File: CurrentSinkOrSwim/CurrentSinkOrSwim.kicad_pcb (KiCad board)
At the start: 2 copper layers, 41.7 x 47.8 mm, 23 parts, among them K101 CONN_3, P101 CONN_2, P102 CONN_2, P301 CONN_1, Q301 BUK7575, U201 LMV358, U401 LM2931ACDG

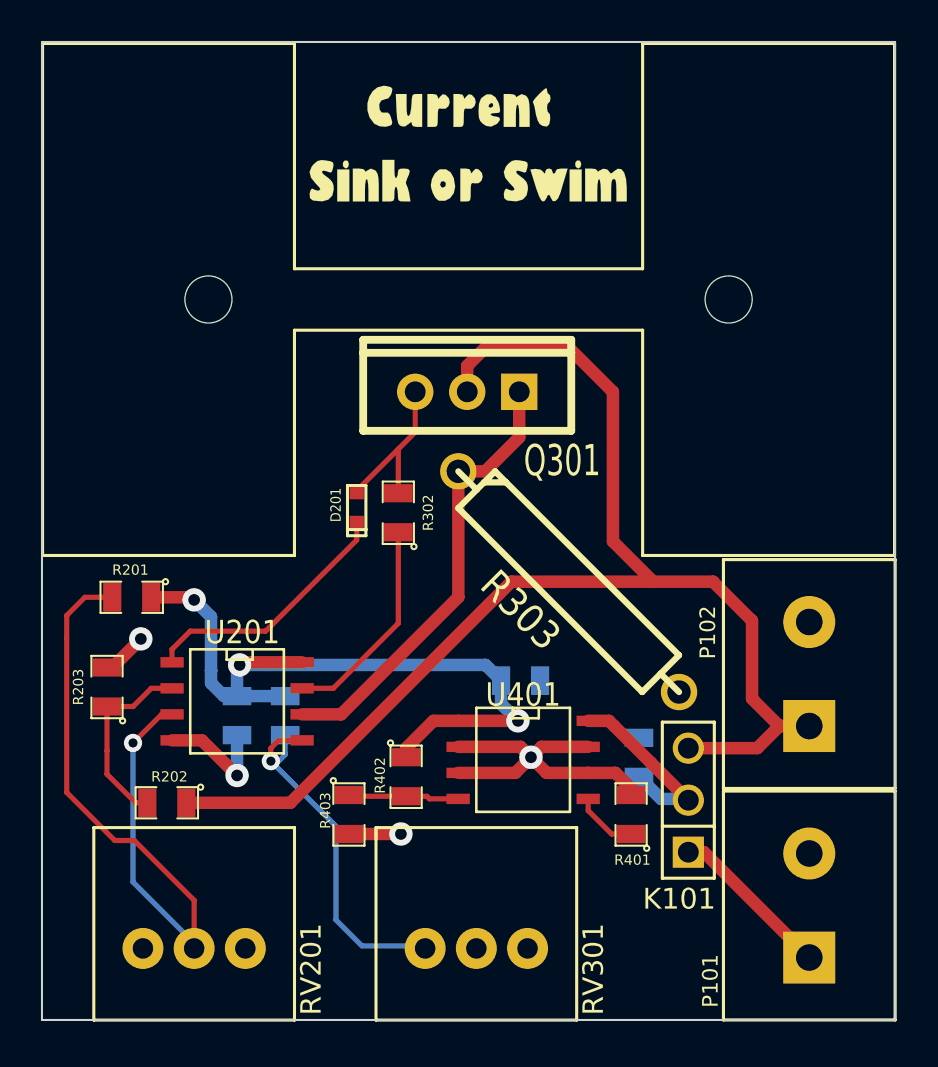
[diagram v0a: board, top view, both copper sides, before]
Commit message: Haciendo algunos cambios porque he tenido que cambiar de componentes y algún valor estaba mal
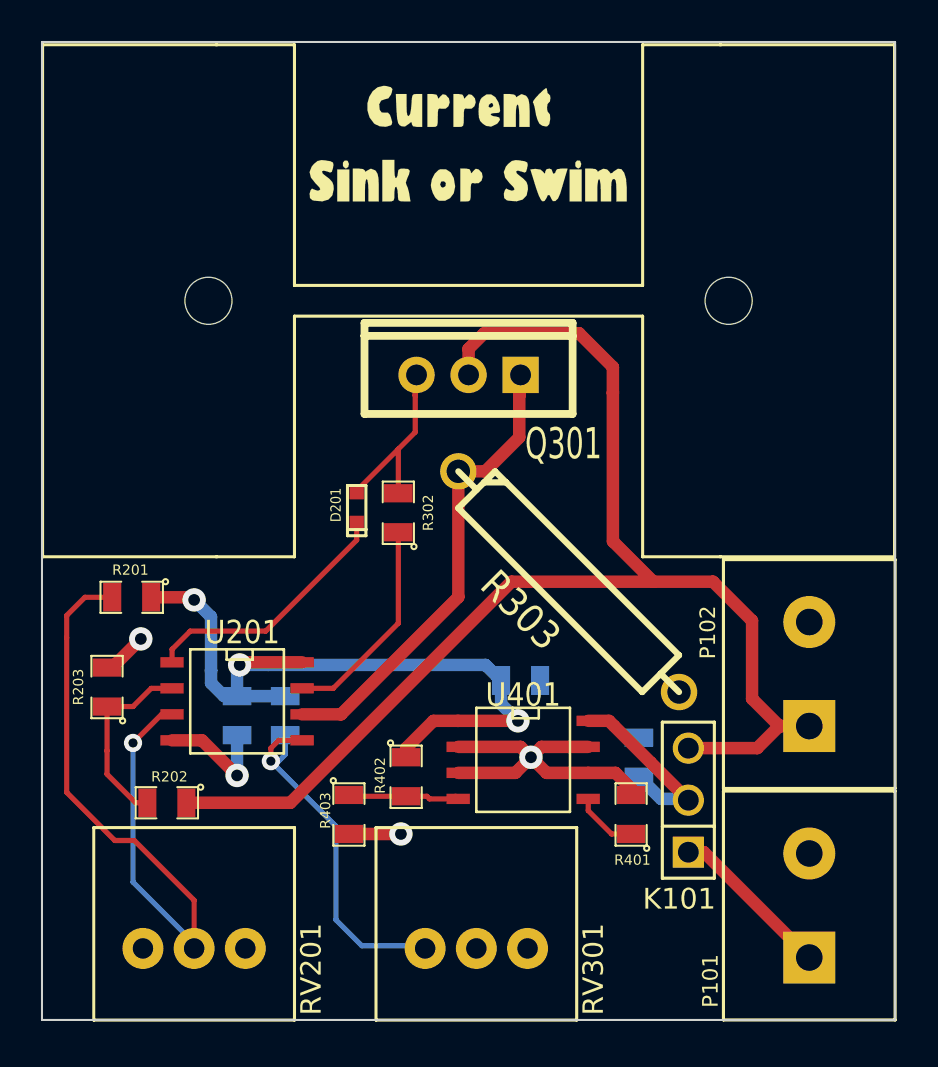
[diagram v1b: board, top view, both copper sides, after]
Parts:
- C301, C401, C402: value C -> .1
- P301: value CONN_1 -> HEATSINK
- R201: value 27,8K -> 28,7K
- moved Q301 0.83 mm to (127.0, 52.1)
- moved P301 0.06 mm to (127.0, 48.5)
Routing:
- net N-0000014: track 22.0 -> 23.1 mm
- net /Current Control/FET_Gate: track 8.29 -> 9.34 mm
- net /Current Control/Current_Sink+: track 66.1 -> 67.1 mm
